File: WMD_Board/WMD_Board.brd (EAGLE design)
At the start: 75.7 x 43.7 mm, 72 parts, among them IC1 FGPMMOPA6H, J1 EMPCB.SMAFSTJ.B.HT, J2 5015680607, Q1 SI2323DS-T1-E3, Q2 SI2323DS-T1-E3, Q3 SI2312BDS, U1 STM32L053C8T6, U2 BSS138, U3 RFM69HCW, U4 BSS138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

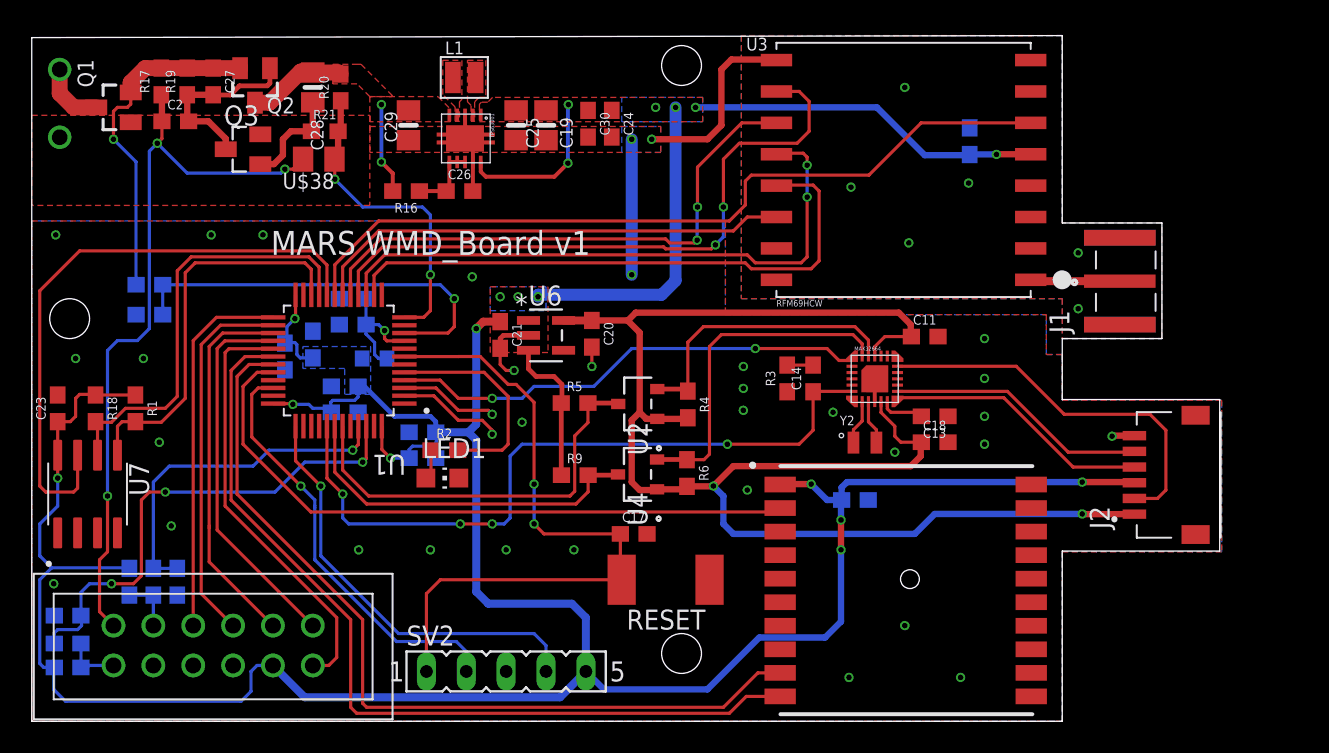
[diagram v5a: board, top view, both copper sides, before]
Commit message: made changes besides zener diode
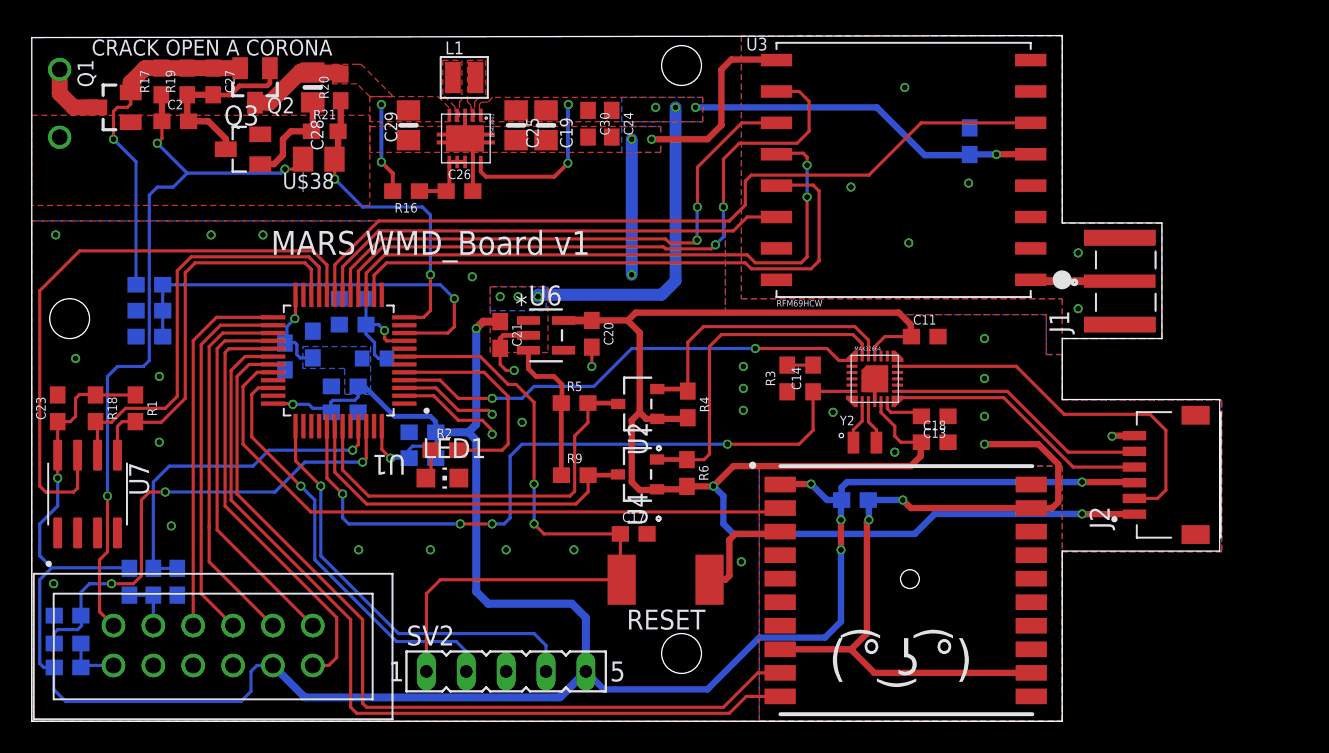
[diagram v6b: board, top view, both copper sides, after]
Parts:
- added C5: 0.1uF, SparkFun-Capacitors:0603
- R1, R18: value 1k -> 4.7k
- R17: value 1k -> 10k
- R19, R20, R7, R8: value 1k -> 100k
- R21: value 1k -> 300k
- moved R8 1.40 mm to (7.49, 24.5)
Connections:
- net GND: now also C5.2
- net N$4: now also C5.1
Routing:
- net GND: track 34.6 -> 88.5 mm, vias 39 -> 38
- net N$4: track 26.0 -> 27.4 mm
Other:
- board text added: "( ͡° ͜ʖ ͡°)"
- board text added: "CRACK OPEN A CORONA"
